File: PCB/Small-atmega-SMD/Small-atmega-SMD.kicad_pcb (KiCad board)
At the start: 2 copper layers, 65.1 x 96.9 mm, 32 parts, among them J1 Daisy port in, J2 ICSP_ISP6, J3 UART, J4 Daisy port out, K1 HYC77-TF09-200, U1 PC817C-S, U2 SE5218, U21 TXB0104QPWRQ1, U3 ATmega328P-AU, Y1 Crystal_GND2

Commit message: Add libraries and update Domino/Angled
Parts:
- C8: value 100n -> 100nF
- K1: footprint MICROSD-HYC77-TF09-200:MICROSD-HYC77-TF09-200 -> HYC04-TF09-200:MICROSD-HYC77-TF09-200
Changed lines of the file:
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@@
 		)
 	)
-	(footprint "MICROSD-HYC77-TF09-200:MICROSD-HYC77-TF09-200"
+	(footprint "HYC04-TF09-200:MICROSD-HYC77-TF09-200"
 		(layer "F.Cu")
 		(at 132.1562 135.0518)
@@
 		)
 		(embedded_fonts no)
-		(model "${KIPRJMOD}/kicad-libs/HYC04-TF09-200.step"
+		(model "HYC04-TF09-200.step"
 			(offset
 				(xyz -7.2 -7.27 1.71)
@@
 			)
 		)
-		(property "Value" "100n"
+		(property "Value" "100nF"
 			(at 0 1.43 0)
 			(layer "F.Fab")
@@
 			)
 		)
-		(property "LCSC" "C1590"
+		(property "LCSC" "C28233"
 			(at 0 0 0)
 			(unlocked yes)
@@
 			)
 		)
-		(property "LCSC" "C3405"
+		(property "LCSC" "C9144"
 			(at 0 0 90)
 			(unlocked yes)
@@
 			)
 		)
-		(property "LCSC" "C15401"
+		(property "LCSC" "C177337"
 			(at 0 0 0)
 			(unlocked yes)

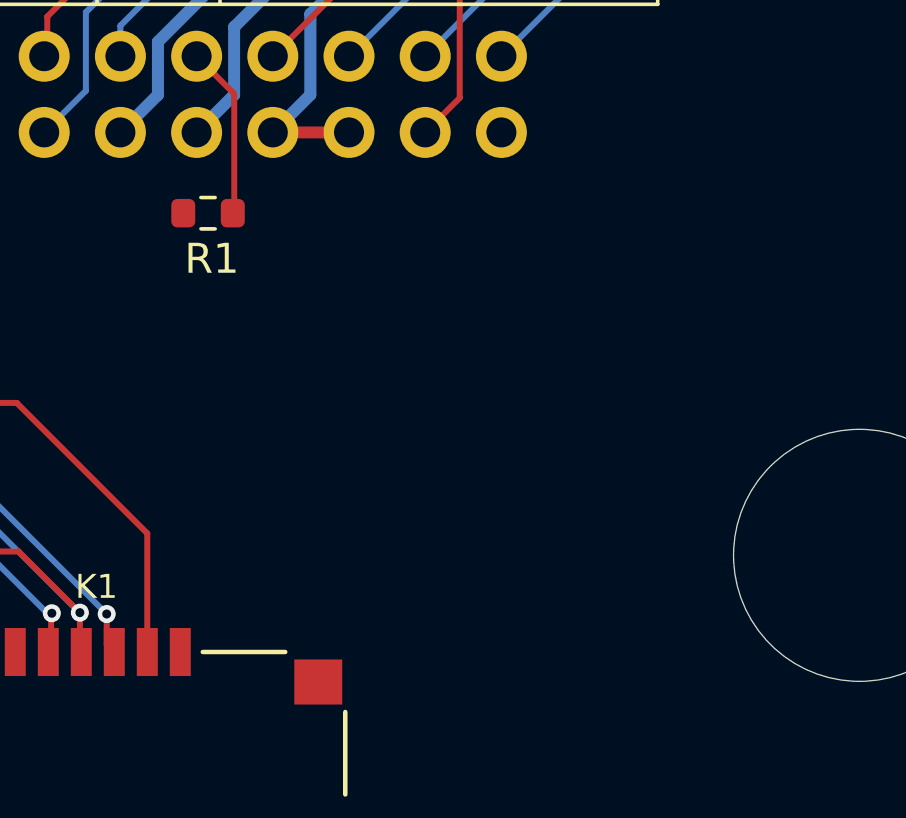
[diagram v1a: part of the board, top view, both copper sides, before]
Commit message: Add logo (thanks to Javier Rivera!!)
Add my own micro/SD modules
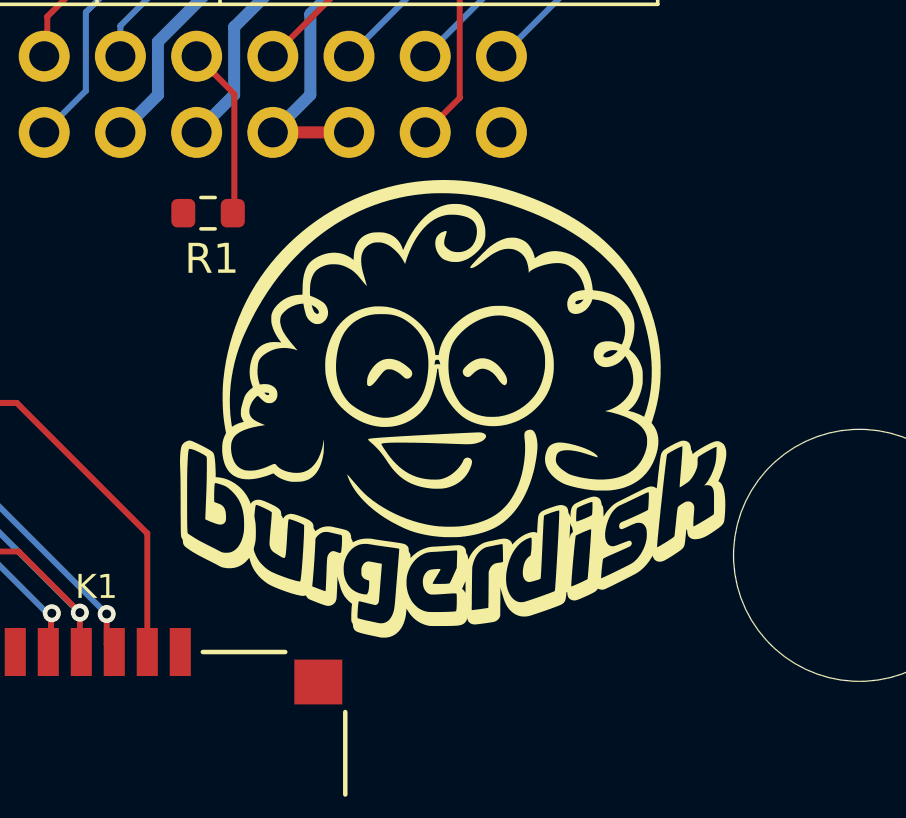
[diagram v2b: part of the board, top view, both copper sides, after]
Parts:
- added G***: LOGO, LOGO, F.Cu at (143.5, 119.3)
- U21: value TXB0104QPWRQ1 -> TXB0104PWR

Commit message: More OCD
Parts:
- renumbered C8 to C1, C4 to C2, C7 to C3, C6 to C4, C3 to C6, C2 to C7, C1 to C8, D3 to D1, D4 to D3, J4 to J1, J1 to J4, R5 to R1, R4 to R2, R7 to R3, R3 to R4, R6 to R5, R1 to R6, R2 to R7, U3 to U2, U2 to U3, U21 to U4
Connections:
- K1 pad SHIELD: (no net) -> GND
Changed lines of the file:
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@@
 		(descr "25-pin D-Sub connector, horizontal/angled (90 deg), THT-mount, female, pitch 2.77x2.84mm, pin-PCB-offset 4.9399999999999995mm, distance of mounting holes 47.1mm, distance of mounting holes to PCB edge 7.4799999999999995mm, see https://disti-assets.s3.amazonaws.com/tonar/files/datasheets/16730.pdf")
 		(tags "25-pin D-Sub connector horizontal angled 90deg THT female pitch 2.77x2.84mm pin-PCB-offset 4.9399999999999995mm mounting-holes-distance 47.1mm mounting-hole-offset 47.1mm")
-		(property "Reference" "J4"
+		(property "Reference" "J1"
 			(at 9.4488 -2.2352 180)
 			(layer "F.SilkS")
@@
 		(descr "Resistor SMD 0603 (1608 Metric), square (rectangular) end terminal, IPC-7351 nominal, (Body size source: IPC-SM-782 page 72, https://www.pcb-3d.com/wordpress/wp-content/uploads/ipc-sm-782a_amendment_1_and_2.pdf), generated with kicad-footprint-generator")
 		(tags "resistor")
-		(property "Reference" "R6"
+		(property "Reference" "R5"
 			(at 2.1844 0.0254 180)
 			(layer "F.SilkS")
@@
 		(descr "SOD-323")
 		(tags "SOD-323")
-		(property "Reference" "D3"
-			(at 0.9652 1.905 180)
+		(property "Reference" "D1"
+			(at -0.2122 1.8884 180)
 			(layer "F.SilkS")
 			(effects
@@
 			(layer "F.Fab")
 		)
-		(fp_text user "K"
-			(at -1.1176 1.4732 180)
-			(layer "F.SilkS")
+		(fp_text user "${REFERENCE}"
+			(at 0 -1.85 90)
+			(layer "F.Fab")
 			(effects
 				(font
@@
 			)
 		)
-		(fp_text user "${REFERENCE}"
-			(at 0 -1.85 90)
+		(fp_text user "K"
+			(at -1.1176 1.4732 180)
 			(layer "F.Fab")
 			(effects
@@
 			(size 1.2 1.5)
 			(layers "F.Cu" "F.Mask" "F.Paste")
+			(net 2 "GND")
+			(pintype "passive")
 		)
 		(pad "SHIELD" smd rect
@@
 			(size 1.2 2.2)
 			(layers "F.Cu" "F.Mask" "F.Paste")
+			(net 2 "GND")
+			(pintype "passive")
 		)
 		(pad "SHIELD" smd rect
@@
 			(size 1.6 1.5)
 			(layers "F.Cu" "F.Mask" "F.Paste")
+			(net 2 "GND")
+			(pintype "passive")
 		)
 		(pad "SHIELD" smd rect
@@
 			(size 1.2 2.2)
 			(layers "F.Cu" "F.Mask" "F.Paste")
+			(net 2 "GND")
+			(pintype "passive")
 		)
 		(embedded_fonts no)
@@
 		(tags "SOP SO")
 		(property "Reference" "U1"
-			(at 6.2212 -1.3878 180)
+			(at -0.0368 3.2492 180)
 			(layer "F.SilkS")
 			(effects
@@
 		(descr "Resistor SMD 0603 (1608 Metric), square (rectangular) end terminal, IPC-7351 nominal, (Body size source: IPC-SM-782 page 72, https://www.pcb-3d.com/wordpress/wp-content/uploads/ipc-sm-782a_amendment_1_and_2.pdf), generated with kicad-footprint-generator")
 		(tags "resistor")
-		(property "Reference" "R1"
+		(property "Reference" "R6"
 			(at 0.127 1.524 0)
 			(layer "F.SilkS")
@@
 		(descr "LED, diameter 3.0mm, 2 pins")
 		(tags "LED diameter 3.0mm 2 pins")
-		(property "Reference" "D4"
-			(at 1.27 -2.96 0)
+		(property "Reference" "D3"
+			(at -2.172 0.0152 0)
 			(layer "F.SilkS")
 			(effects
@@
 		(descr "Capacitor SMD 0603 (1608 Metric), square (rectangular) end terminal, IPC-7351 nominal, (Body size source: IPC-SM-782 page 76, https://www.pcb-3d.com/wordpress/wp-content/uploads/ipc-sm-782a_amendment_1_and_2.pdf), generated with kicad-footprint-generator")
 		(tags "capacitor")
-		(property "Reference" "C3"
+		(property "Reference" "C6"
 			(at -2.6038 0 0)
 			(layer "F.SilkS")
@@
 		(descr "32-Lead Plastic Thin Quad Flatpack (PT) - 7x7x1.0 mm Body, 2.00 mm [TQFP] (see Microchip Packaging Specification 00000049BS.pdf)")
 		(tags "QFP 0.8")
-		(property "Reference" "U3"
-			(at -6.369 -4.5638 180)
+		(property "Reference" "U2"
+			(at -4.442 -4.968 180)
 			(layer "F.SilkS")
 			(effects
@@
 		(tags "Through hole pin header THT 1x02 2.54mm single row")
 		(property "Reference" "J3"
-			(at -2.54 -1.0668 180)
+			(at -2.507 1.0554 180)
 			(layer "F.SilkS")
 			(effects
@@
 		(descr "Capacitor SMD 0603 (1608 Metric), square (rectangular) end terminal, IPC_7351 nominal, (Body size source: IPC-SM-782 page 76, https://www.pcb-3d.com/wordpress/wp-content/uploads/ipc-sm-782a_amendment_1_and_2.pdf), generated with kicad-footprint-generator")
 		(tags "capacitor")
-		(property "Reference" "C8"
-			(at -2.4638 -0.0508 0)
+		(property "Reference" "C1"
+			(at 0.0014 1.5304 0)
 			(layer "F.SilkS")
 			(effects
@@
 		(descr "Resistor SMD 1206 (3216 Metric), square (rectangular) end terminal, IPC_7351 nominal, (Body size source: IPC-SM-782 page 72, https://www.pcb-3d.com/wordpress/wp-content/uploads/ipc-sm-782a_amendment_1_and_2.pdf), generated with kicad-footprint-generator")
 		(tags "resistor")
-		(property "Reference" "R3"
+		(property "Reference" "R4"
 			(at -3.048 -0.0254 0)
 			(layer "F.SilkS")
@@
 		(descr "Resistor SMD 0603 (1608 Metric), square (rectangular) end terminal, IPC-7351 nominal, (Body size source: IPC-SM-782 page 72, https://www.pcb-3d.com/wordpress/wp-content/uploads/ipc-sm-782a_amendment_1_and_2.pdf), generated with kicad-footprint-generator")
 		(tags "resistor")
-		(property "Reference" "R4"
+		(property "Reference" "R2"
 			(at 2.3368 0.127 180)
 			(layer "F.SilkS")
@@
 		(descr "Capacitor SMD 0603 (1608 Metric), square (rectangular) end terminal, IPC-7351 nominal, (Body size source: IPC-SM-782 page 76, https://www.pcb-3d.com/wordpress/wp-content/uploads/ipc-sm-782a_amendment_1_and_2.pdf), generated with kicad-footprint-generator")
 		(tags "capacitor")
-		(property "Reference" "C1"
+		(property "Reference" "C8"
 			(at -2.5908 0.0254 0)
 			(layer "F.SilkS")
@@
 		(descr "Capacitor SMD 0603 (1608 Metric), square (rectangular) end terminal, IPC-7351 nominal, (Body size source: IPC-SM-782 page 76, https://www.pcb-3d.com/wordpress/wp-content/uploads/ipc-sm-782a_amendment_1_and_2.pdf), generated with kicad-footprint-generator")
 		(tags "capacitor")
-		(property "Reference" "C4"
+		(property "Reference" "C2"
 			(at 2.1082 0.0762 0)
 			(layer "F.SilkS")
@@
 		(descr "Capacitor SMD 0603 (1608 Metric), square (rectangular) end terminal, IPC-7351 nominal, (Body size source: IPC-SM-782 page 76, https://www.pcb-3d.com/wordpress/wp-content/uploads/ipc-sm-782a_amendment_1_and_2.pdf), generated with kicad-footprint-generator")
 		(tags "capacitor")
-		(property "Reference" "C7"
+		(property "Reference" "C3"
 			(at -2.1968 -0.0756 180)
 			(layer "F.SilkS")
@@
 		(descr "14-Lead Plastic Thin Shrink Small Outline (ST)-4.4 mm Body [TSSOP] with exposed pad (http://cds.linear.com/docs/en/datasheet/34301fa.pdf)")
 		(tags "SSOP 0.65 exposed pad")
-		(property "Reference" "U21"
-			(at -4.687 -1.5124 180)
+		(property "Reference" "U4"
+			(at -4.7956 0.2858 180)
 			(layer "F.SilkS")
 			(effects
@@
 		(descr "Through hole IDC box header, 2x10, 2.54mm pitch, DIN 41651 / IEC 60603-13, double rows, https://docs.google.com/spreadsheets/d/16SsEcesNF15N3Lb4niX7dcUr-NY5_MFPQhobNuNppn4/edit#gid=0")
 		(tags "Through hole horizontal IDC box header THT 2x10 2.54mm double row")
-		(property "Reference" "J1"
+		(property "Reference" "J4"
 			(at -0.0762 -2.0828 180)
 			(layer "F.SilkS")
@@
 		(tags "SOD-323F")
 		(property "Reference" "D2"
-			(at -0.7874 1.651 0)
+			(at -0.0592 1.6276 0)
 			(layer "F.SilkS")
 			(effects
@@
 		(descr "Resistor SMD 0603 (1608 Metric), square (rectangular) end terminal, IPC-7351 nominal, (Body size source: IPC-SM-782 page 72, https://www.pcb-3d.com/wordpress/wp-content/uploads/ipc-sm-782a_amendment_1_and_2.pdf), generated with kicad-footprint-generator")
 		(tags "resistor")
-		(property "Reference" "R2"
-			(at 0 -1.43 0)
+		(property "Reference" "R7"
+			(at 2.4518 0.0268 0)
 			(layer "F.SilkS")
 			(effects
@@
 		(tags "Through hole vertical IDC box header THT 2x03 2.54mm double row")
 		(property "Reference" "J2"
-			(at 6.9596 9.9568 180)
+			(at 6.6924 2.6814 180)
 			(layer "F.SilkS")
 			(effects
@@
 		(descr "Capacitor SMD 0603 (1608 Metric), square (rectangular) end terminal, IPC-7351 nominal, (Body size source: IPC-SM-782 page 76, https://www.pcb-3d.com/wordpress/wp-content/uploads/ipc-sm-782a_amendment_1_and_2.pdf), generated with kicad-footprint-generator")
 		(tags "capacitor")
-		(property "Reference" "C6"
+		(property "Reference" "C4"
 			(at -2.159 -0.0248 180)
 			(layer "F.SilkS")
@@
 		(descr "Resistor SMD 0603 (1608 Metric), square (rectangular) end terminal, IPC_7351 nominal, (Body size source: IPC-SM-782 page 72, https://www.pcb-3d.com/wordpress/wp-content/uploads/ipc-sm-782a_amendment_1_and_2.pdf), generated with kicad-footprint-generator")
 		(tags "resistor")
-		(property "Reference" "R7"
-			(at -2.5278 0.0254 0)
+		(property "Reference" "R3"
+			(at 0.0468 -1.4008 0)
 			(layer "F.SilkS")
 			(effects
@@
 		(descr "Resistor SMD 0603 (1608 Metric), square (rectangular) end terminal, IPC-7351 nominal, (Body size source: IPC-SM-782 page 72, https://www.pcb-3d.com/wordpress/wp-content/uploads/ipc-sm-782a_amendment_1_and_2.pdf), generated with kicad-footprint-generator")
 		(tags "resistor")
-		(property "Reference" "R5"
-			(at 0.6096 1.397 180)
+		(property "Reference" "R1"
+			(at 0.0448 1.4114 180)
 			(layer "F.SilkS")
 			(effects
@@
 		(descr "Capacitor SMD 0603 (1608 Metric), square (rectangular) end terminal, IPC-7351 nominal, (Body size source: IPC-SM-782 page 76, https://www.pcb-3d.com/wordpress/wp-content/uploads/ipc-sm-782a_amendment_1_and_2.pdf), generated with kicad-footprint-generator")
 		(tags "capacitor")
-		(property "Reference" "C2"
+		(property "Reference" "C7"
 			(at -2.6038 -0.0762 0)
 			(layer "F.SilkS")
@@
 		(descr "SOT, 5 Pin (JEDEC MO-178 Var AA https://www.jedec.org/document_search?search_api_views_fulltext=MO-178), generated with kicad-footprint-generator ipc_gullwing_generator.py")
 		(tags "SOT TO_SOT_SMD")
-		(property "Reference" "U2"
-			(at 1.1739 2.3246 0)
+		(property "Reference" "U3"
+			(at 0.1669 2.3246 0)
 			(layer "F.SilkS")
 			(effects

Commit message: More OCD
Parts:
- Y1: value Crystal_GND2 -> Resonator_GND2
- moved C2 8.76 mm to (109.0, 103.2)
- moved C1 8.67 mm to (128.3, 74.8), turned to 90 degrees
- moved R2 1.61 mm to (138.7, 61.2), turned to 0 degrees
- moved J3 1.29 mm to (114.2, 72.8)
- moved D1 1.08 mm to (143.9, 57.8), turned to 0 degrees
- moved R5 0.89 mm to (112.0, 106.5), turned to 180 degrees
- renumbered C5 to C2, C2 to C3, C3 to C4, C4 to C5
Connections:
- net RDDATA_in renamed RDDATA
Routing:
- net GND: track 51.1 -> 67.4 mm, vias 14 -> 11
- net PH3_in: track 38.9 -> 44.2 mm
- net 3V3: track 55.4 -> 52.1 mm, vias 3 -> 0
- net 5V_burgerDisk: track 110.0 -> 107.9 mm
- net CS_L: track 36.3 -> 34.7 mm, vias 0 -> 2
- net HDSEL_out: track 29.1 -> 30.5 mm
- net MISO_L: track 27.3 -> 28.6 mm
- net OE: track 2.92 -> 1.76 mm
- net MOSI: track 67.4 -> 68.2 mm
- net DRV1_in: track 58.2 -> 58.9 mm
- net Net-(D3-A): track 3.51 -> 2.81 mm
- net SCLK_L: track 30.1 -> 30.8 mm
- net Net-(R1-Pad2): track 9.90 -> 10.5 mm
- net TX: track 11.0 -> 11.6 mm
- net DRV1_out: track 34.6 -> 35.1 mm

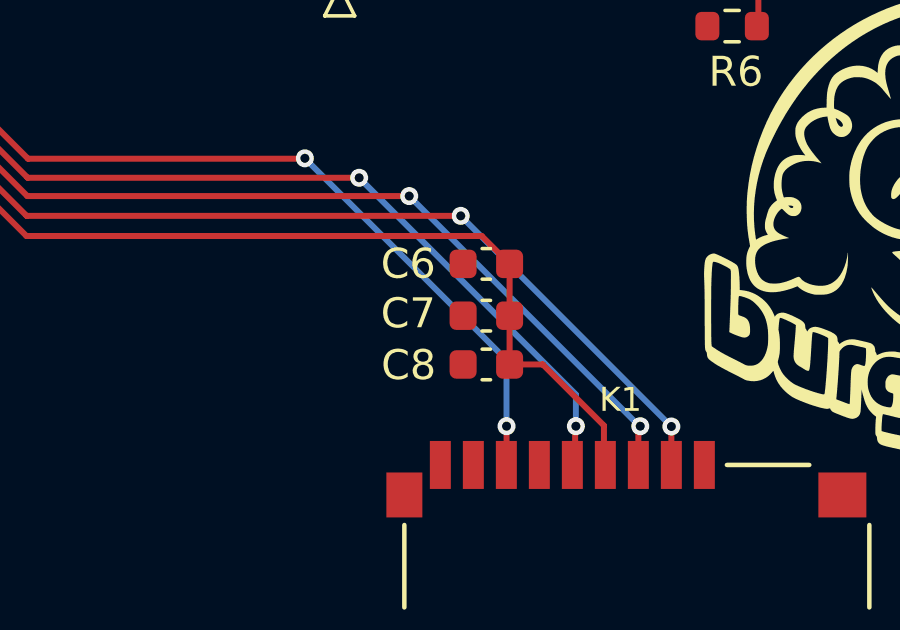
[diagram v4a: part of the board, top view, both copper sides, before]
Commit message: Fix microSD caps
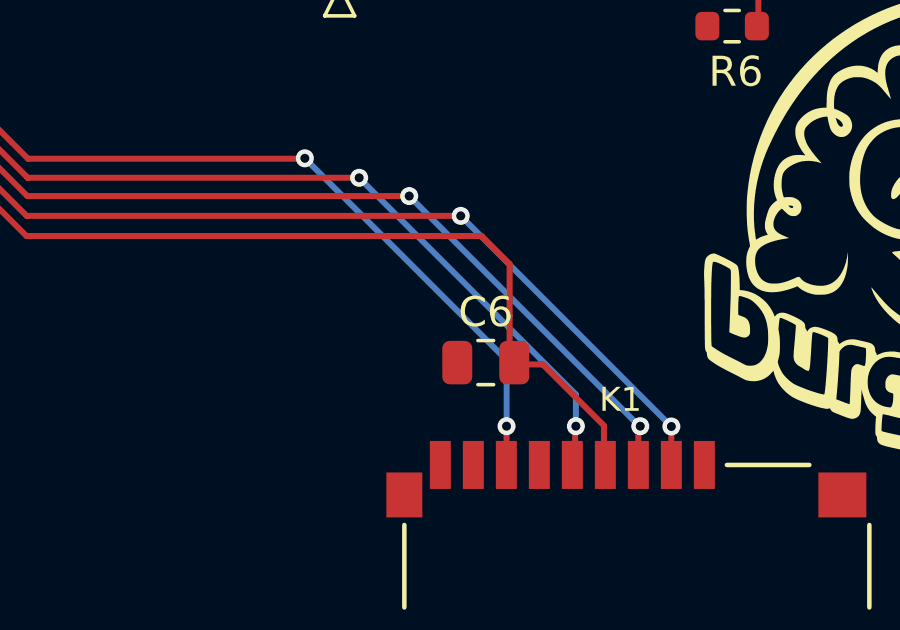
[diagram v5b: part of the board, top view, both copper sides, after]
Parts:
- removed C7: 100n, Capacitor_SMD:C_0603_1608Metric
- removed C8: 2u2, Capacitor_SMD:C_0603_1608Metric
- C6: value 100n -> 22uf; footprint Capacitor_SMD:C_0603_1608Metric -> Capacitor_SMD:C_0805_2012Metric
- moved C6 3.29 mm to (127.1, 123.9)
